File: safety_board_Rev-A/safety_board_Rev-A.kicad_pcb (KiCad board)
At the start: 2 copper layers, 110 x 20 mm, 21 parts, among them J1 24V_switched, J2 amp_A, J4 amp_B, J6 GND, J8 out_B, J9 out_A, K1 FINDER-40.52, Q1 2N7000

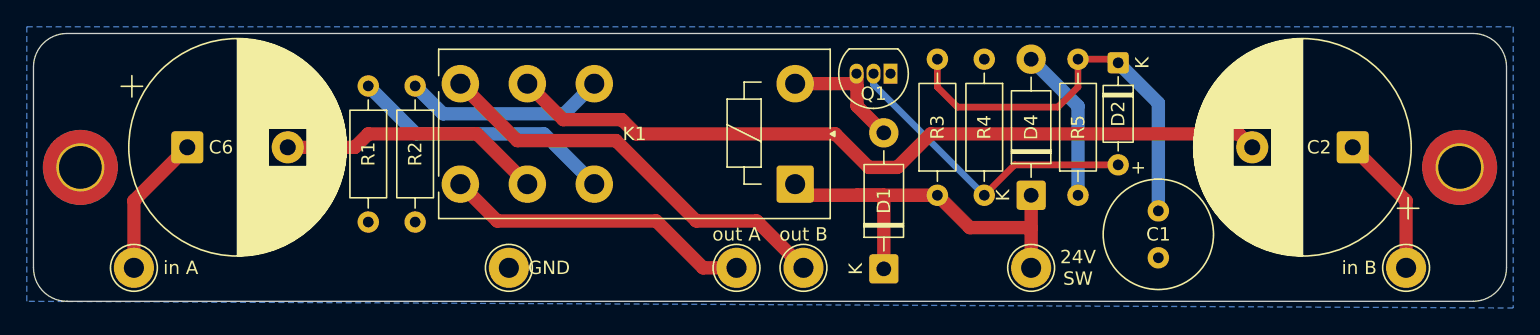
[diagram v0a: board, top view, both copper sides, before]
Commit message: Added images for the turn-on delay board, visual modifications to schematic.
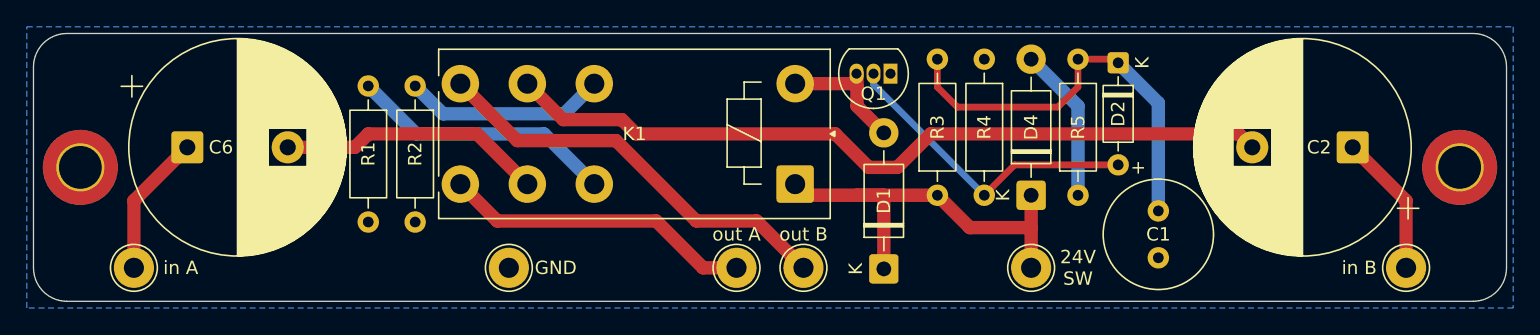
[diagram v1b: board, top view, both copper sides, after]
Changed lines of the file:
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@@
 	)
 	(gr_text "GND"
-		(at 133.5 110 0)
+		(at 134 110 0)
 		(layer "F.SilkS")
 		(effects
@@
 		(polygon
 			(pts
-				(xy 94.5 92) (xy 205.5 92) (xy 205.5 113) (xy 94.5 112.5)
+				(xy 94.5 92) (xy 205.5 92) (xy 205.5 113) (xy 94.5 113)
 			)
 		)
